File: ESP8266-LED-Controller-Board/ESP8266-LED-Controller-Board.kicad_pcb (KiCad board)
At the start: 2 copper layers, 70 x 38 mm, 55 parts, among them J1 Barrel_Jack_Switch, J2 USB_C_Receptacle_USB2.0, J3 Conn_01x04_Male, J4 Conn_01x05_Male, J5 Screw_Terminal_01x04, J6 Screw_Terminal_01x02, Q1 NTD5867NLT4G, Q2 NTD5867NLT4G, Q3 NTD5867NLT4G, Q4 NTD5867NLT4G, Q5 NTD5867NLT4G, SW1 SW_Push, SW2 SW_Push, U1 TPS563200, U2 ACS70331EESATR-005U3, U3 ESP-12F, U4 SN74LV1T34DCKR, U5 SN74LV1T34DCKR

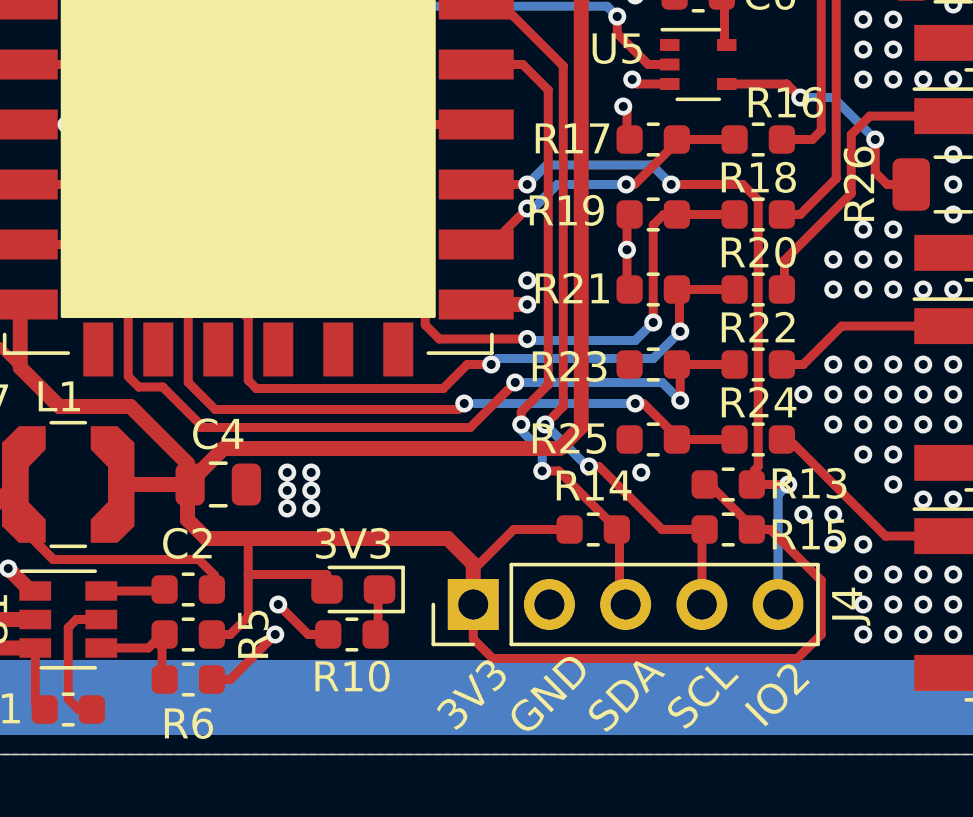
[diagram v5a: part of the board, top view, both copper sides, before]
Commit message: Added temperature sensors.
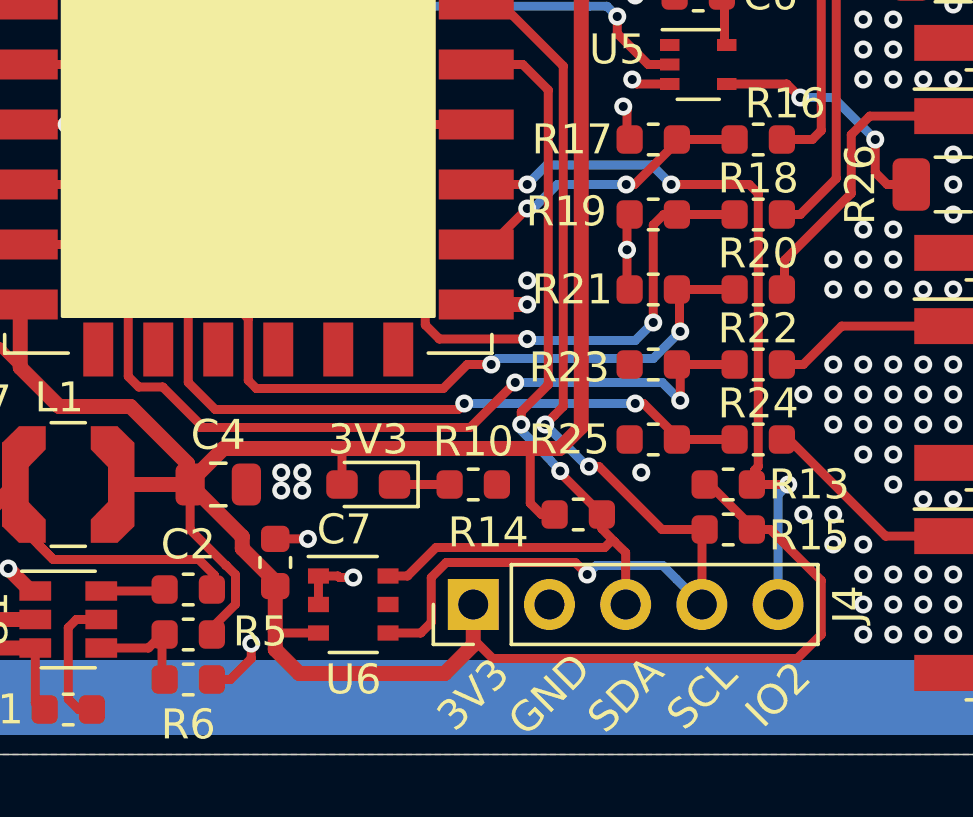
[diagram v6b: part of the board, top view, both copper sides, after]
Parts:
- added C7: 100n, Capacitor_SMD:C_0603_1608Metric, F.Cu at (126.4, 81.6)
- added U6: PCT2075GVX‎, Package_SO:TSOP-6_1.65x3.05mm_P0.95mm, F.Cu at (129.0, 83.0)
- moved R10 6.43 mm to (133.0, 79.0), turned to 0 degrees
- moved 3V3 3.54 mm to (129.5, 79.0)
- moved R14 0.71 mm to (136.5, 80.0)
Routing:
- net /I2C_SCL: track 25.1 -> 38.3 mm, vias 2 -> 3
- net /I2C_SDA: track 22.1 -> 29.7 mm
- net +3V3: track 123.4 -> 125.6 mm
- net GND: track 28.9 -> 29.5 mm, vias 161 -> 160

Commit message: Updated for manufacturing.
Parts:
- moved R11 0.90 mm to (114.7, 63.0)
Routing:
- net /PIXEL_DATA_3V3-LED_G_CTRL: track 52.2 -> 56.9 mm
- net /PIXEL_CLK_3V3-LED_B_CTRL: track 54.9 -> 57.2 mm
- net +3V3: track 125.6 -> 126.3 mm
- net /BOOT: track 36.1 -> 36.8 mm
